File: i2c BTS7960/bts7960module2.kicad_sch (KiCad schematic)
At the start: 42 parts, among them J3 jst, J4 Conn_01x04, U1 74AHC244, U2 BTS7960B, U3 BTS7960B, U4 BTS7960B, U6 BTS7960B

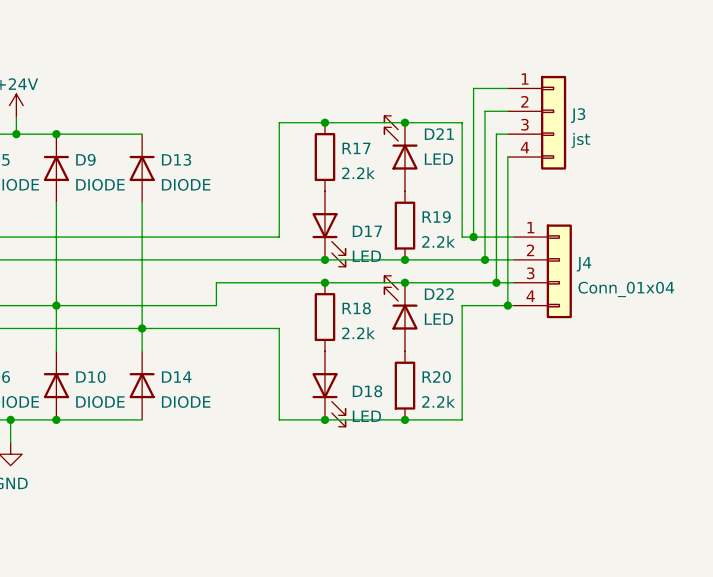
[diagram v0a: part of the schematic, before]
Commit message: tweaked buck converter hole sizes and silk
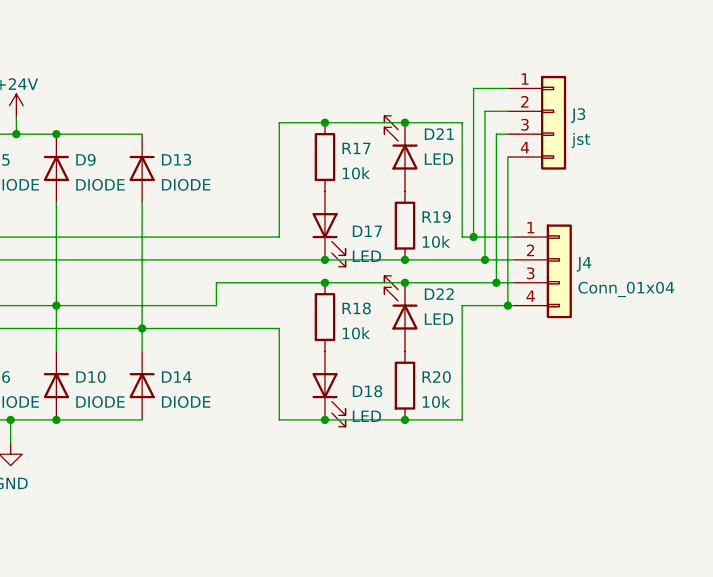
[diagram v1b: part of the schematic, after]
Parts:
- R17, R18, R19, R20: value 2.2k -> 10k
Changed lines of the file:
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@@
       (effects (font (size 1.27 1.27)) (justify left))
     )
-    (property "Value" "2.2k" (id 1) (at 253.238 121.2466 0)
+    (property "Value" "10k" (id 1) (at 253.238 121.2466 0)
       (effects (font (size 1.27 1.27)) (justify left))
     )
@@
       (effects (font (size 1.27 1.27)) (justify left))
     )
-    (property "Value" "2.2k" (id 1) (at 253.238 103.4666 0)
+    (property "Value" "10k" (id 1) (at 253.238 103.4666 0)
       (effects (font (size 1.27 1.27)) (justify left))
     )
@@
       (effects (font (size 1.27 1.27)) (justify left))
     )
-    (property "Value" "2.2k" (id 1) (at 244.348 95.8466 0)
+    (property "Value" "10k" (id 1) (at 244.348 95.8466 0)
       (effects (font (size 1.27 1.27)) (justify left))
     )
@@
       (effects (font (size 1.27 1.27)) (justify left))
     )
-    (property "Value" "2.2k" (id 1) (at 244.348 113.6266 0)
-      (effects (font (size 1.27 1.27)) (justify left))
-    )
+    (property "Value" "10k" (id 1) (at 244.348 113.6266 0)
+      (effects (font (size 1.27 1.27)) (justify left))
+    )

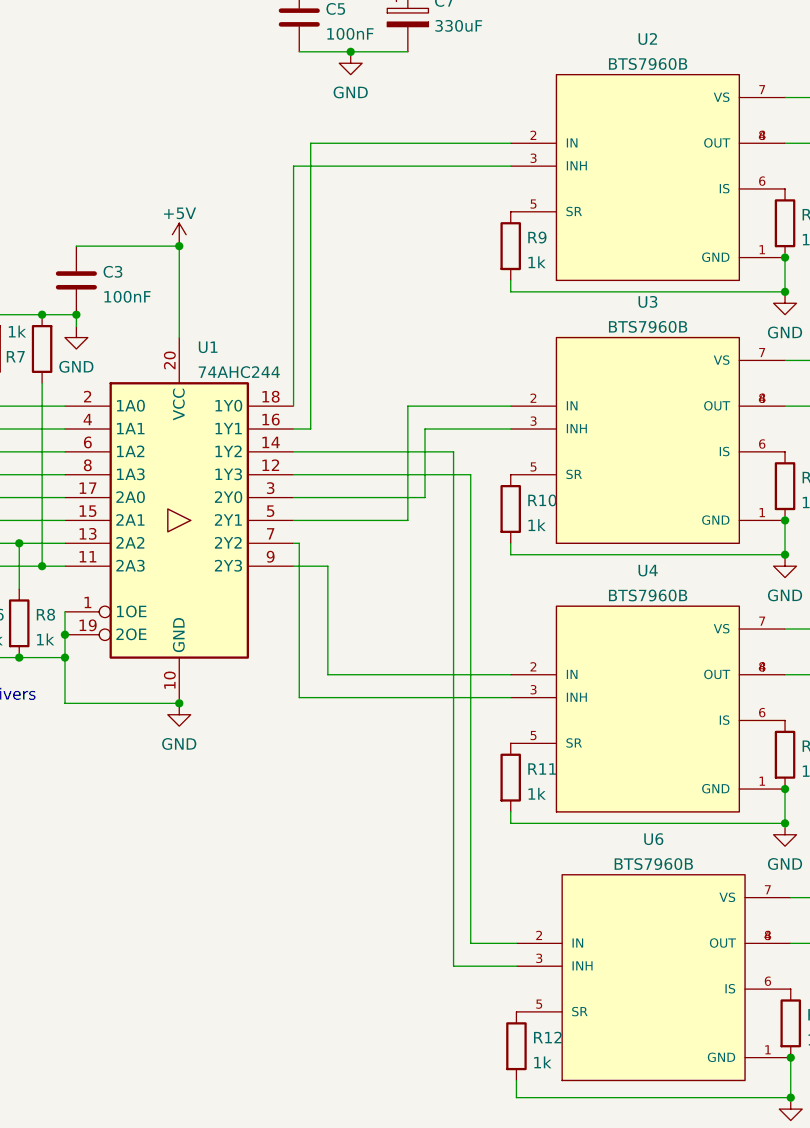
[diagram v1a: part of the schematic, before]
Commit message: reel detent added
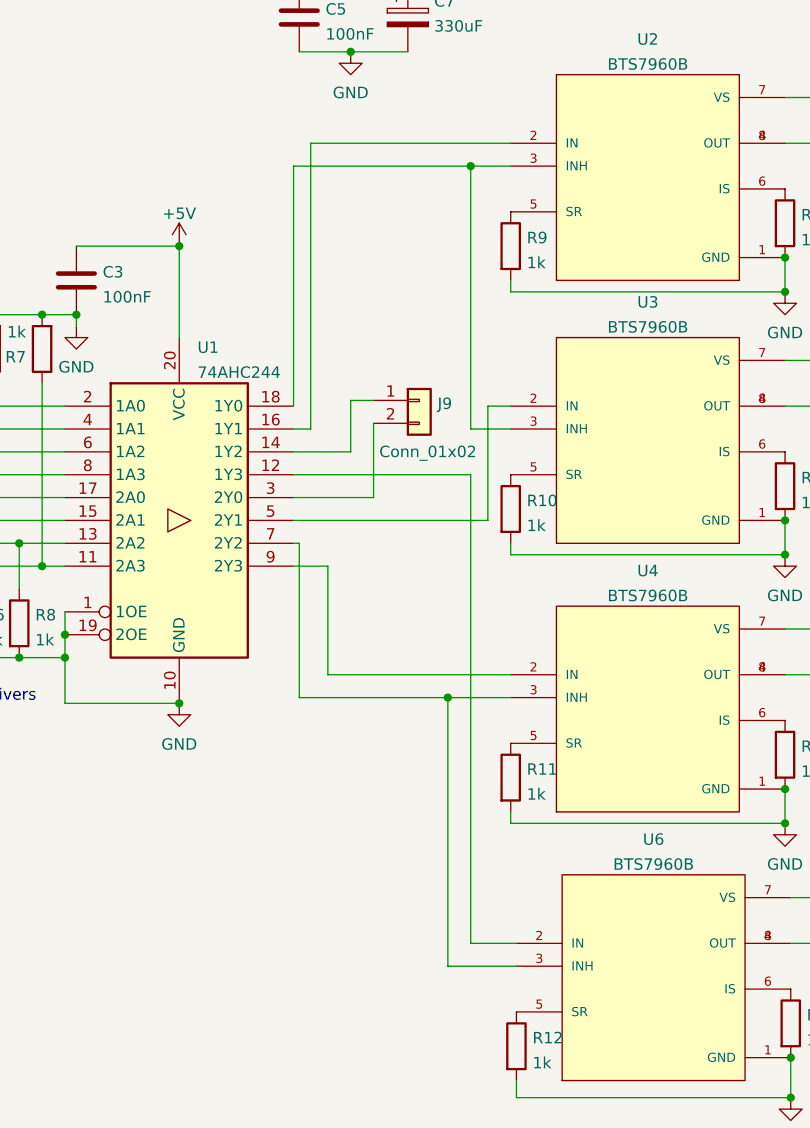
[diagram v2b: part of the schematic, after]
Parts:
- added J9: Conn_01x02, Connector_PinHeader_2.54mm:PinHeader_2x01_P2.54mm_Vertical, symbol Connector_Generic:Conn_01x02
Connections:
- net at U1.7 (2Y2), U4.3 (INH): now also U6.3 (INH)
- net at U1.18 (1Y0), U2.3 (INH): now also U3.3 (INH)
- net at U1.14 (1Y2): now also J9.1 (Pin_1); no longer U6.3 (INH)
- net at U1.3 (2Y0): now also J9.2 (Pin_2); no longer U3.3 (INH)
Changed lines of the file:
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@@
   (junction (at 172.72 63.5) (diameter 0) (color 0 0 0 0)
   )
+  (junction (at 137.795 53.34) (diameter 0) (color 0 0 0 0)
+  )
   (junction (at 212.725 123.19) (diameter 0) (color 0 0 0 0)
   )
@@
   (junction (at 84.455 69.85) (diameter 0) (color 0 0 0 0)
   )
+  (junction (at 135.255 112.395) (diameter 0) (color 0 0 0 0)
+  )
   (junction (at 81.915 90.17) (diameter 0) (color 0 0 0 0)
   )
@@
     (stroke (width 0) (type default) (color 0 0 0 0))
   )
+  (wire (pts (xy 142.875 142.24) (xy 135.255 142.24))
+    (stroke (width 0) (type default) (color 0 0 0 0))
+  )
   (wire (pts (xy 261.62 107.95) (xy 263.525 107.95))
     (stroke (width 0) (type default) (color 0 0 0 0))
@@
     (stroke (width 0) (type default) (color 0 0 0 0))
   )
-  (wire (pts (xy 118.745 112.395) (xy 142.24 112.395))
+  (wire (pts (xy 118.745 112.395) (xy 135.255 112.395))
     (stroke (width 0) (type default) (color 0 0 0 0))
   )
@@
     (stroke (width 0) (type default) (color 0 0 0 0))
   )
+  (wire (pts (xy 118.11 85.09) (xy 124.46 85.09))
+    (stroke (width 0) (type default) (color 0 0 0 0))
+  )
   (wire (pts (xy 242.57 105.41) (xy 251.46 105.41))
     (stroke (width 0) (type default) (color 0 0 0 0))
@@
     (stroke (width 0) (type default) (color 0 0 0 0))
   )
-  (wire (pts (xy 130.81 80.01) (xy 130.81 92.71))
+  (wire (pts (xy 139.7 80.01) (xy 139.7 92.71))
     (stroke (width 0) (type default) (color 0 0 0 0))
   )
@@
     (stroke (width 0) (type default) (color 0 0 0 0))
   )
-  (wire (pts (xy 130.81 80.01) (xy 142.24 80.01))
+  (wire (pts (xy 139.7 80.01) (xy 142.24 80.01))
     (stroke (width 0) (type default) (color 0 0 0 0))
   )
@@
     (stroke (width 0) (type default) (color 0 0 0 0))
   )
-  (wire (pts (xy 130.81 92.71) (xy 118.11 92.71))
+  (wire (pts (xy 139.7 92.71) (xy 118.11 92.71))
     (stroke (width 0) (type default) (color 0 0 0 0))
   )
@@
     (stroke (width 0) (type default) (color 0 0 0 0))
   )
+  (wire (pts (xy 127 90.17) (xy 118.11 90.17))
+    (stroke (width 0) (type default) (color 0 0 0 0))
+  )
+  (wire (pts (xy 137.795 82.55) (xy 137.795 53.34))
+    (stroke (width 0) (type default) (color 0 0 0 0))
+  )
   (wire (pts (xy 180.975 74.93) (xy 180.975 104.775))
     (stroke (width 0) (type default) (color 0 0 0 0))
@@
     (stroke (width 0) (type default) (color 0 0 0 0))
   )
+  (wire (pts (xy 137.795 53.34) (xy 142.24 53.34))
+    (stroke (width 0) (type default) (color 0 0 0 0))
+  )
   (wire (pts (xy 118.11 87.63) (xy 137.795 87.63))
     (stroke (width 0) (type default) (color 0 0 0 0))
@@
     (stroke (width 0) (type default) (color 0 0 0 0))
   )
-  (wire (pts (xy 118.11 85.09) (xy 135.89 85.09))
+  (wire (pts (xy 124.46 85.09) (xy 124.46 79.375))
+    (stroke (width 0) (type default) (color 0 0 0 0))
+  )
+  (wire (pts (xy 124.46 79.375) (xy 127 79.375))
     (stroke (width 0) (type default) (color 0 0 0 0))
   )
@@
     (stroke (width 0) (type default) (color 0 0 0 0))
   )
+  (wire (pts (xy 135.255 142.24) (xy 135.255 112.395))
+    (stroke (width 0) (type default) (color 0 0 0 0))
+  )
   (wire (pts (xy 185.42 110.49) (xy 212.725 110.49))
     (stroke (width 0) (type default) (color 0 0 0 0))
@@
     (stroke (width 0) (type default) (color 0 0 0 0))
   )
-  (wire (pts (xy 118.11 53.34) (xy 142.24 53.34))
+  (wire (pts (xy 118.11 53.34) (xy 137.795 53.34))
     (stroke (width 0) (type default) (color 0 0 0 0))
   )
@@
     (stroke (width 0) (type default) (color 0 0 0 0))
   )
+  (wire (pts (xy 142.24 82.55) (xy 137.795 82.55))
+    (stroke (width 0) (type default) (color 0 0 0 0))
+  )
   (wire (pts (xy 180.975 38.1) (xy 180.975 45.72))
     (stroke (width 0) (type default) (color 0 0 0 0))
@@
     (stroke (width 0) (type default) (color 0 0 0 0))
   )
-  (wire (pts (xy 132.715 90.17) (xy 132.715 82.55))
-    (stroke (width 0) (type default) (color 0 0 0 0))
-  )
   (wire (pts (xy 257.81 90.17) (xy 251.46 90.17))
     (stroke (width 0) (type default) (color 0 0 0 0))
@@
     (stroke (width 0) (type default) (color 0 0 0 0))
   )
-  (wire (pts (xy 118.11 90.17) (xy 132.715 90.17))
-    (stroke (width 0) (type default) (color 0 0 0 0))
-  )
   (wire (pts (xy 237.49 123.19) (xy 242.57 123.19))
     (stroke (width 0) (type default) (color 0 0 0 0))
@@
     (stroke (width 0) (type default) (color 0 0 0 0))
   )
-  (wire (pts (xy 132.715 82.55) (xy 142.24 82.55))
-    (stroke (width 0) (type default) (color 0 0 0 0))
-  )
   (wire (pts (xy 251.46 107.95) (xy 261.62 107.95))
     (stroke (width 0) (type default) (color 0 0 0 0))
@@
     (stroke (width 0) (type default) (color 0 0 0 0))
   )
-  (wire (pts (xy 135.89 142.24) (xy 135.89 85.09))
-    (stroke (width 0) (type default) (color 0 0 0 0))
-  )
   (wire (pts (xy 263.525 102.87) (xy 259.08 102.87))
     (stroke (width 0) (type default) (color 0 0 0 0))
@@
     (stroke (width 0) (type default) (color 0 0 0 0))
   )
+  (wire (pts (xy 135.255 112.395) (xy 142.24 112.395))
+    (stroke (width 0) (type default) (color 0 0 0 0))
+  )
   (wire (pts (xy 180.975 45.72) (xy 180.975 74.93))
     (stroke (width 0) (type default) (color 0 0 0 0))
@@
     (stroke (width 0) (type default) (color 0 0 0 0))
   )
+  (wire (pts (xy 127 81.915) (xy 127 90.17))
+    (stroke (width 0) (type default) (color 0 0 0 0))
+  )
   (wire (pts (xy 67.945 85.09) (xy 76.2 85.09))
     (stroke (width 0) (type default) (color 0 0 0 0))
@@
   )
   (wire (pts (xy 257.81 102.87) (xy 257.81 90.17))
-    (stroke (width 0) (type default) (color 0 0 0 0))
-  )
-  (wire (pts (xy 135.89 142.24) (xy 142.875 142.24))
     (stroke (width 0) (type default) (color 0 0 0 0))
   )
@@
     )
     (pin "1")
+    (pin "2")
+  )
+  (symbol (lib_id "Connector_Generic:Conn_01x02") (at 132.08 79.375 0) (unit 1)
+    (in_bom yes) (on_board yes)
+    (property "Reference" "J9" (id 0) (at 134.112 79.7365 0)
+      (effects (font (size 1.27 1.27)) (justify left))
+    )
+    (property "Value" "Conn_01x02" (id 1) (at 127.635 85.09 0)
+      (effects (font (size 1.27 1.27)) (justify left))
+    )
+    (property "Footprint" "Connector_PinHeader_2.54mm:PinHeader_2x01_P2.54mm_Vertical" (id 2) (at 132.08 79.375 0)
+      (effects (font (size 1.27 1.27)) hide)
+    )
+    (property "Datasheet" "~" (id 3) (at 132.08 79.375 0)
+      (effects (font (size 1.27 1.27)) hide)
+    )
+    (pin "1")
